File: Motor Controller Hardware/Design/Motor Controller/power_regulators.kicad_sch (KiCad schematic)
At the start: 26 parts, among them J32 Conn_01x04_Pin, U18 AZ1084-5.0, U19 AZ1084-5.0, U20 AZ1084-3.3, U32 LMR38020

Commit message: A
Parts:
- J32: footprint Connector_JST:JST_EH_B4B-EH-A_1x04_P2.50mm_Vertical -> Connector:FanPinHeader_1x04_P2.54mm_Vertical
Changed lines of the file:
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@@
 			)
 		)
-		(property "Footprint" "Connector_JST:JST_EH_B4B-EH-A_1x04_P2.50mm_Vertical"
+		(property "Footprint" "Connector:FanPinHeader_1x04_P2.54mm_Vertical"
 			(at 209.55 58.42 0)
 			(effects

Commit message: A
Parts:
- removed C110, C111: 10u, Capacitor_SMD:C_0805_2012Metric, symbol Device:C
- removed C113: 100u, Capacitor_SMD:CP_Elec_6.3x9.9, symbol Device:C_Polarized
- removed U18: AZ1084-5.0, Package_TO_SOT_SMD:TO-252-2, symbol Regulator_Linear:AZ1084-5.0

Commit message: AS
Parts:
- R105: footprint (none) -> Resistor_SMD:R_0603_1608Metric
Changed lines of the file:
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@@
 			)
 		)
-		(property "Footprint" ""
+		(property "Footprint" "Resistor_SMD:R_0603_1608Metric"
 			(at 59.182 77.47 90)
 			(effects

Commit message: A:
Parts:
- added C68: 100u, Capacitor_SMD:CP_Elec_6.3x9.9, symbol Device:C_Polarized
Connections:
- net +5V: now also C68.1
- net GND: now also C68.2
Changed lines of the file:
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@@
 	)
 	(junction
+		(at 184.15 153.67)
+		(diameter 0)
+		(color 0 0 0 0)
+	)
+	(junction
 		(at 124.46 66.04)
 		(diameter 0)
@@
 	(wire
 		(pts
+			(xy 193.04 153.67) (xy 184.15 153.67)
+		)
+		(stroke
+			(width 0)
+			(type default)
+		)
+	)
+	(wire
+		(pts
 			(xy 25.4 128.27) (xy 36.83 128.27)
 		)
@@
 	(wire
 		(pts
+			(xy 193.04 144.78) (xy 193.04 142.24)
+		)
+		(stroke
+			(width 0)
+			(type default)
+		)
+	)
+	(wire
+		(pts
 			(xy 92.71 66.04) (xy 111.76 66.04)
 		)
@@
 	(wire
 		(pts
+			(xy 193.04 142.24) (xy 184.15 142.24)
+		)
+		(stroke
+			(width 0)
+			(type default)
+		)
+	)
+	(wire
+		(pts
 			(xy 144.78 73.66) (xy 144.78 66.04)
 		)
@@
 	(wire
 		(pts
+			(xy 193.04 152.4) (xy 193.04 153.67)
+		)
+		(stroke
+			(width 0)
+			(type default)
+		)
+	)
+	(wire
+		(pts
 			(xy 92.71 71.12) (xy 114.3 71.12)
 		)
@@
 					(unit 1)
 				)
+			)
+		)
+	)
+	(symbol
+		(lib_id "Device:C_Polarized")
+		(at 193.04 148.59 0)
+		(mirror y)
+		(unit 1)
+		(exclude_from_sim no)
+		(in_bom yes)
+		(on_board yes)
+		(dnp no)
+		(property "Reference" "C68"
+			(at 196.342 155.702 0)
+			(effects
+				(font
+					(size 1.27 1.27)
+				)
+				(justify left)
+			)
+		)
+		(property "Value" "100u"
+			(at 196.342 158.242 0)
+			(effects
+				(font
+					(size 1.27 1.27)
+				)
+				(justify left)
+			)
+		)
+		(property "Footprint" "Capacitor_SMD:CP_Elec_6.3x9.9"
+			(at 192.0748 152.4 0)
+			(effects
+				(font
+					(size 1.27 1.27)
+				)
+				(hide yes)
+			)
+		)
+		(property "Datasheet" "~"
+			(at 193.04 148.59 0)
+			(effects
+				(font
+					(size 1.27 1.27)
+				)
+				(hide yes)
+			)
+		)
+		(property "Description" "Polarized capacitor"
+			(at 193.04 148.59 0)
+			(effects
+				(font
+					(size 1.27 1.27)
+				)
+				(hide yes)
+			)
+		)
+		(property "LCSC Part#" ""
+			(at 193.04 148.59 0)
+			(effects
+				(font
+					(size 1.27 1.27)
+				)
+				(hide yes)
+			)
+		)
+		(pin "2"
+		)
+		(pin "1"
+		)
+		(instances
+			(project "Motor Controller"
+				(path "/480a1464-7c70-42e1-b2f7-69e659e11383/6ad1cc71-da87-4814-be84-3c7a7f59eef6/fed1da5e-34a3-4d0d-8847-1b884dfe4f39"
+					(reference "C68")
+					(unit 1)
+				)

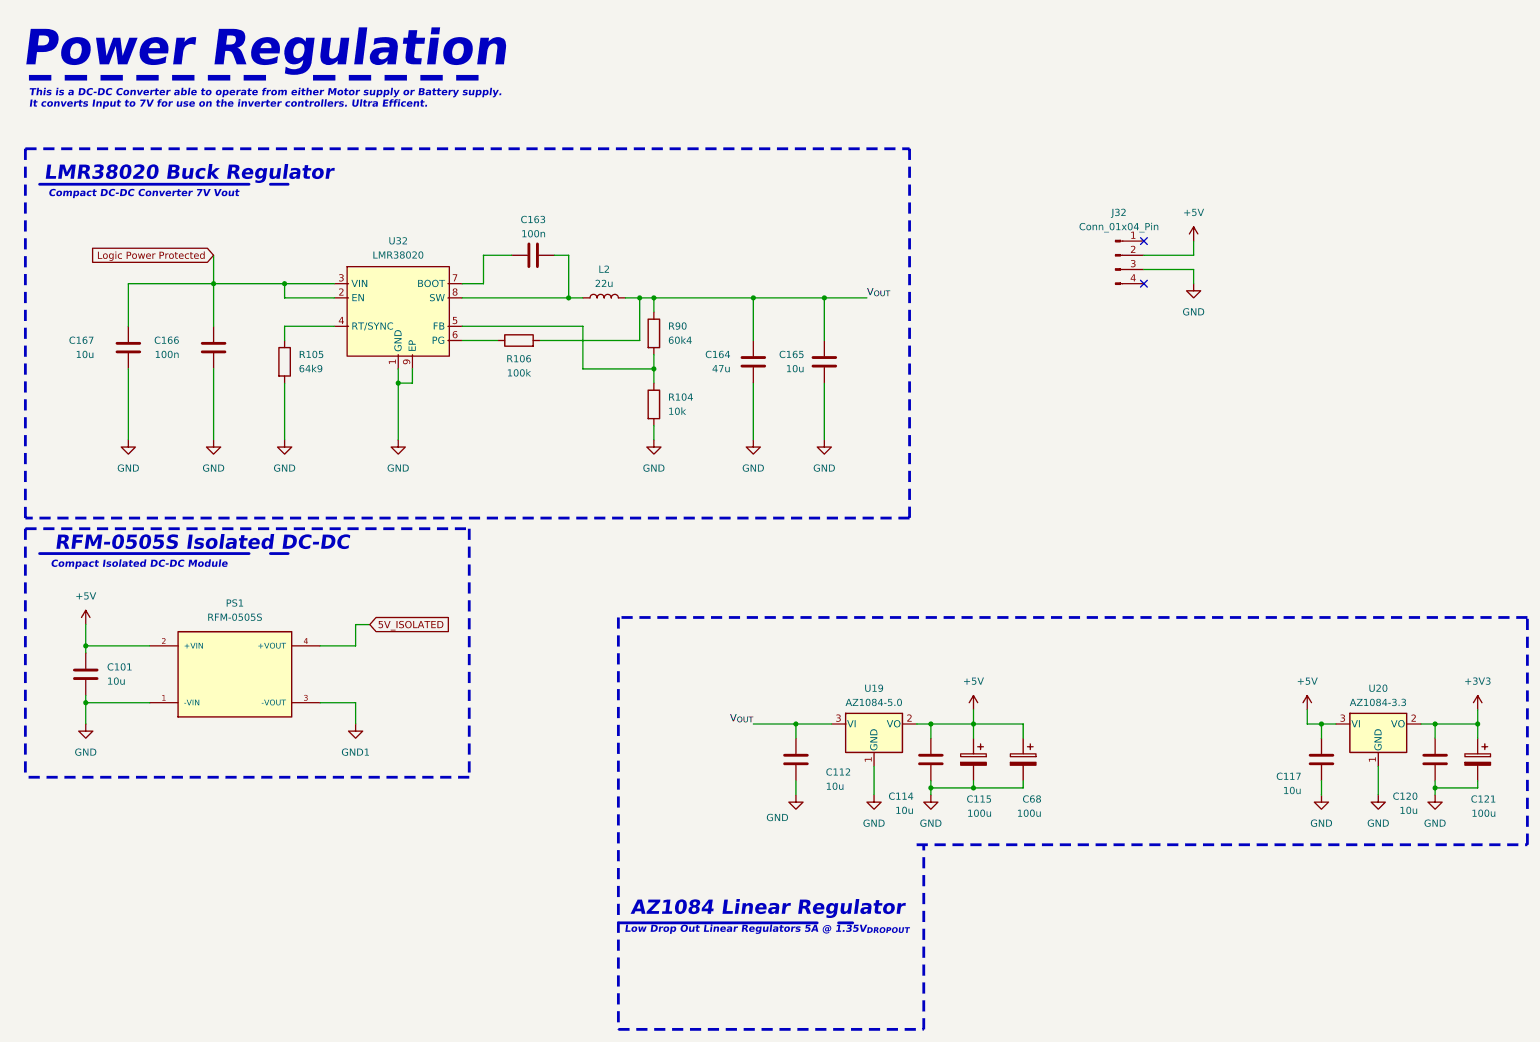
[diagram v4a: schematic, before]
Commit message: Changed size to 120x100 and routing 90%
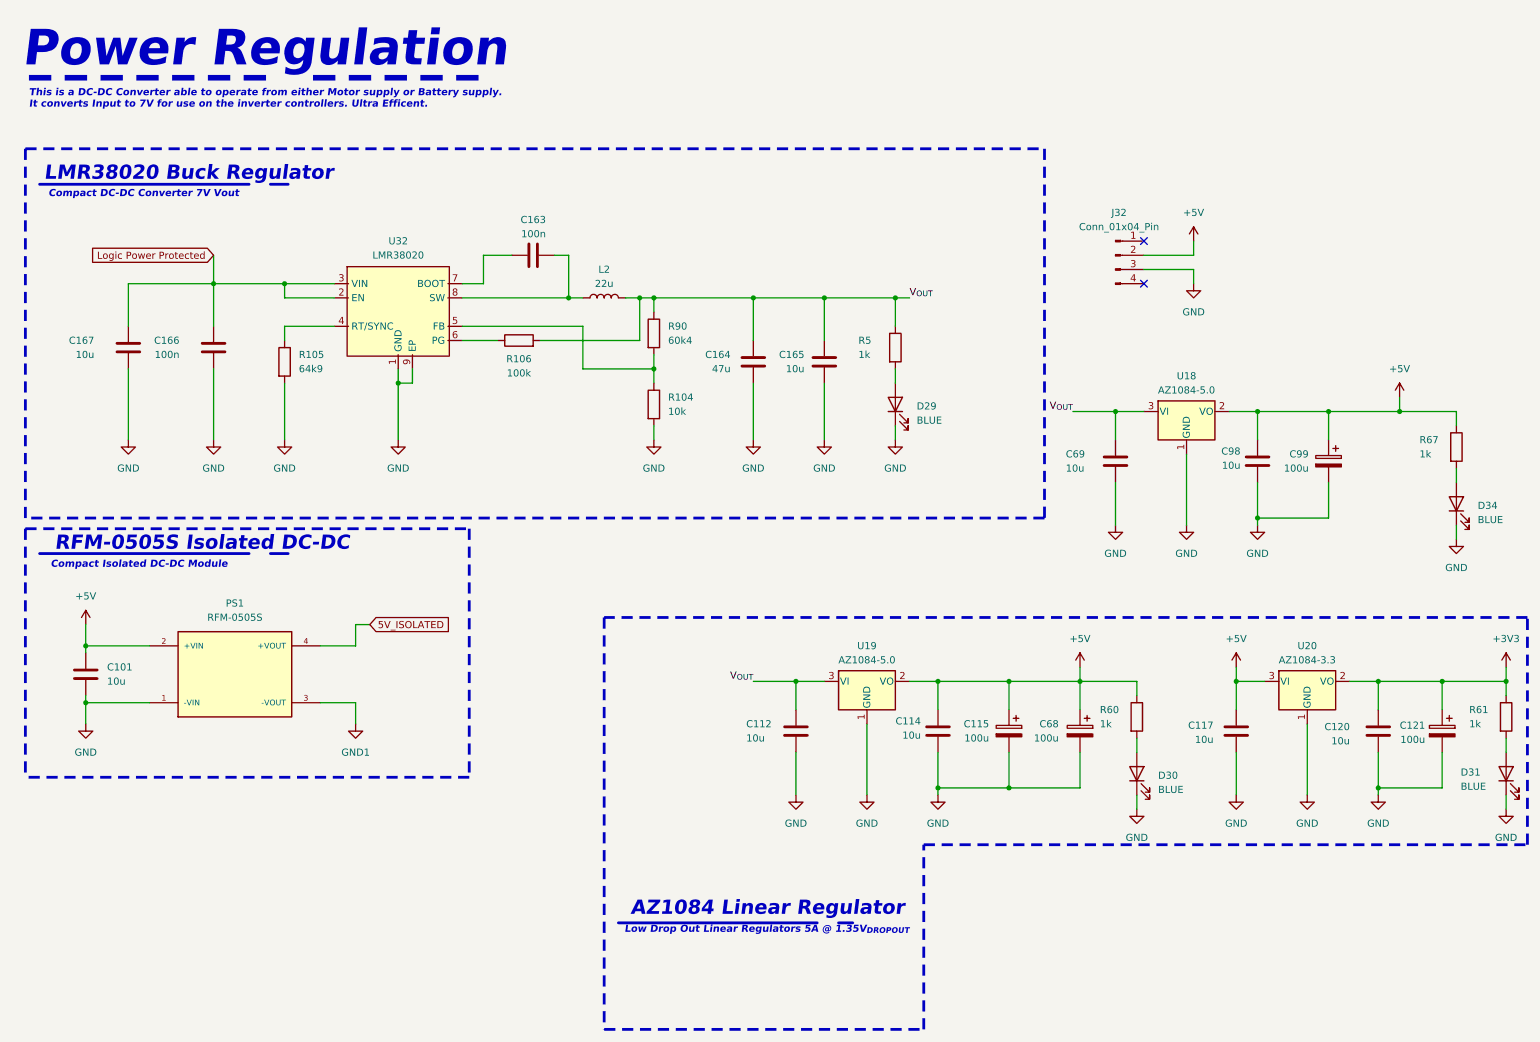
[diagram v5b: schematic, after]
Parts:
- added C69, C98: 10u, Capacitor_SMD:C_0805_2012Metric, symbol Device:C
- added C99: 100u, Capacitor_SMD:CP_Elec_6.3x9.9, symbol Device:C_Polarized
- added D29, D30, D31, D34: BLUE, LED_SMD:LED_0603_1608Metric, symbol Device:LED
- added R5, R60, R61, R67: 1k, Resistor_SMD:R_0603_1608Metric, symbol Device:R
- added U18: AZ1084-5.0, Package_TO_SOT_SMD:TO-252-2, symbol Regulator_Linear:AZ1084-5.0
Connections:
- net +3V3: now also R61.1
- net +5V: now also C98.1, C99.1, R60.1, R67.1, U18.2 (VO)
- net GND: now also C69.2, C98.2, C99.2, D29.1 (K), D30.1 (K), D31.1 (K), D34.1 (K), U18.1 (GND)
- net V_{OUT}: now also C69.1, R5.1, U18.3 (VI)
- new net: D34.2 (A), R67.2
- new net: D30.2 (A), R60.2
- new net: D31.2 (A), R61.2
- new net: D29.2 (A), R5.2
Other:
- moved on the sheet: C112, C114, C115, C117, C120, C121, C68, U19, U20

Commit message: A
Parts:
- removed C69, C98: 10u, Capacitor_SMD:C_0805_2012Metric, symbol Device:C
- removed C99: 100u, Capacitor_SMD:CP_Elec_6.3x9.9, symbol Device:C_Polarized
- removed D34: BLUE, LED_SMD:LED_0603_1608Metric, symbol Device:LED
- removed R67: 1k, Resistor_SMD:R_0603_1608Metric, symbol Device:R
- removed U18: AZ1084-5.0, Package_TO_SOT_SMD:TO-252-2, symbol Regulator_Linear:AZ1084-5.0
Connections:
- net V_{OUT} renamed +12V
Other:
- moved on the sheet: C112, C114, C115, C117, C120, C121, C68, D30, D31, J32, R60, R61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

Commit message: A
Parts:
- J32: value Conn_01x04_Pin -> Fan
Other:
- moved on the sheet: J32
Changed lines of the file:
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@@
 	)
 	(no_connect
-		(at 100.33 165.1)
+		(at 31.75 171.45)
 	)
 	(no_connect
-		(at 100.33 172.72)
+		(at 31.75 179.07)
 	)
 	(wire
@@
 	(wire
 		(pts
-			(xy 109.22 170.18) (xy 100.33 170.18)
+			(xy 40.64 176.53) (xy 31.75 176.53)
 		)
 		(stroke
@@
 	(wire
 		(pts
-			(xy 109.22 172.72) (xy 109.22 170.18)
+			(xy 40.64 179.07) (xy 40.64 176.53)
 		)
 		(stroke
@@
 	(wire
 		(pts
-			(xy 109.22 167.64) (xy 100.33 167.64)
+			(xy 40.64 173.99) (xy 31.75 173.99)
 		)
 		(stroke
@@
 	(wire
 		(pts
-			(xy 109.22 165.1) (xy 109.22 167.64)
+			(xy 40.64 171.45) (xy 40.64 173.99)
 		)
 		(stroke
@@
 	(symbol
 		(lib_id "Connector:Conn_01x04_Pin")
-		(at 95.25 167.64 0)
+		(at 26.67 173.99 0)
 		(unit 1)
 		(exclude_from_sim no)
@@
 		(fields_autoplaced yes)
 		(property "Reference" "J32"
-			(at 95.885 160.02 0)
+			(at 27.305 166.37 0)
 			(effects
 				(font
@@
 			)
 		)
-		(property "Value" "Conn_01x04_Pin"
-			(at 95.885 162.56 0)
+		(property "Value" "Fan"
+			(at 27.305 168.91 0)
 			(effects
 				(font
@@
 		)
 		(property "Footprint" "Connector:FanPinHeader_1x04_P2.54mm_Vertical"
-			(at 95.25 167.64 0)
+			(at 26.67 173.99 0)
 			(effects
 				(font
@@
 		)
 		(property "Datasheet" "~"
-			(at 95.25 167.64 0)
+			(at 26.67 173.99 0)
 			(effects
 				(font
@@
 		)
 		(property "Description" "Generic connector, single row, 01x04, script generated"
-			(at 95.25 167.64 0)
+			(at 26.67 173.99 0)
 			(effects
 				(font
@@
 	(symbol
 		(lib_id "power:+5V")
-		(at 109.22 165.1 0)
+		(at 40.64 171.45 0)
 		(unit 1)
 		(exclude_from_sim no)
@@
 		(fields_autoplaced yes)
 		(property "Reference" "#PWR0178"
-			(at 109.22 168.91 0)
+			(at 40.64 175.26 0)
 			(effects
 				(font
@@
 		)
 		(property "Value" "+5V"
-			(at 109.22 160.02 0)
+			(at 40.64 166.37 0)
 			(effects
 				(font
@@
 		)
 		(property "Footprint" ""
-			(at 109.22 165.1 0)
+			(at 40.64 171.45 0)
 			(effects
 				(font
@@
 		)
 		(property "Datasheet" ""
-			(at 109.22 165.1 0)
+			(at 40.64 171.45 0)
 			(effects
 				(font
@@
 		)
 		(property "Description" "Power symbol creates a global label with name \"+5V\""
-			(at 109.22 165.1 0)
+			(at 40.64 171.45 0)
 			(effects
 				(font
@@
 	(symbol
 		(lib_id "power:GND")
-		(at 109.22 172.72 0)
+		(at 40.64 179.07 0)
 		(unit 1)
 		(exclude_from_sim no)
@@
 		(fields_autoplaced yes)
 		(property "Reference" "#PWR0179"
-			(at 109.22 179.07 0)
+			(at 40.64 185.42 0)
 			(effects
 				(font
@@
 		)
 		(property "Value" "GND"
-			(at 109.22 177.8 0)
+			(at 40.64 184.15 0)
 			(effects
 				(font
@@
 		)
 		(property "Footprint" ""
-			(at 109.22 172.72 0)
+			(at 40.64 179.07 0)
 			(effects
 				(font
@@
 		)
 		(property "Datasheet" ""
-			(at 109.22 172.72 0)
+			(at 40.64 179.07 0)
 			(effects
 				(font
@@
 		)
 		(property "Description" "Power symbol creates a global label with name \"GND\" , ground"
-			(at 109.22 172.72 0)
+			(at 40.64 179.07 0)
 			(effects
 				(font

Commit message: A
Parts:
- C101: LCSC# (none) -> C5156756
- C112, C114, C117, C120, C165, C167: LCSC# (none) -> C15850
- C115, C121, C68: LCSC# (none) -> C72478
- C163: LCSC# (none) -> C476766
- C164: LCSC# (none) -> C16780
- C166: LCSC Part# (none) -> C88219; LCSC# (none) -> C88219
- L2: footprint ecocad_lib_footprints:IND_SPM7054VC-220M-D -> Inductor_SMD:L_SXN_SMDRI127
- U19: LCSC# (none) -> C2980701
- U20: LCSC# (none) -> C151391
